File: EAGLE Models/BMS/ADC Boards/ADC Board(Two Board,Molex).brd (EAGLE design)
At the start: 77.5 x 64.4 mm, 34 parts, among them IC1 ADS7956, IC2 ADS7956, IC3 ADS7956, X1 6_PIN_CONNTE_IDC, X10 6_PIN_CONNTE_IDC, X11 6_PIN_CONNTE_IDC, X12 6_PIN_CONNTE_IDC, X2 6_PIN_CONNTE_IDC, X3 6_PIN_CONNTE_IDC, X4 6_PIN_CONNTE_IDC, X5 6_PIN_CONNTE_IDC, X6 6_PIN_CONNTE_IDC, X7 8_PIN_CONN

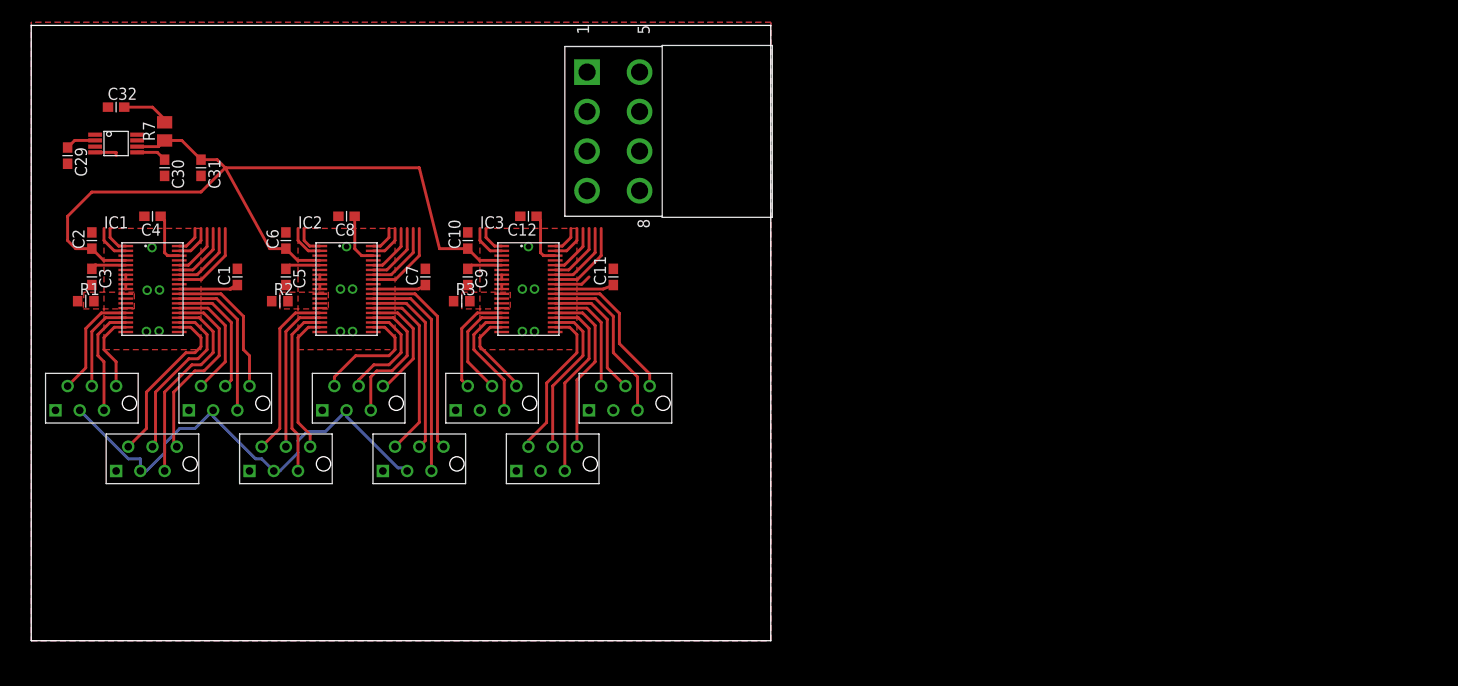
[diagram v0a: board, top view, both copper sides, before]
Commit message: Switched connectors, preparing to add dedicated analog power supply, Completed first revision of temp sense boards
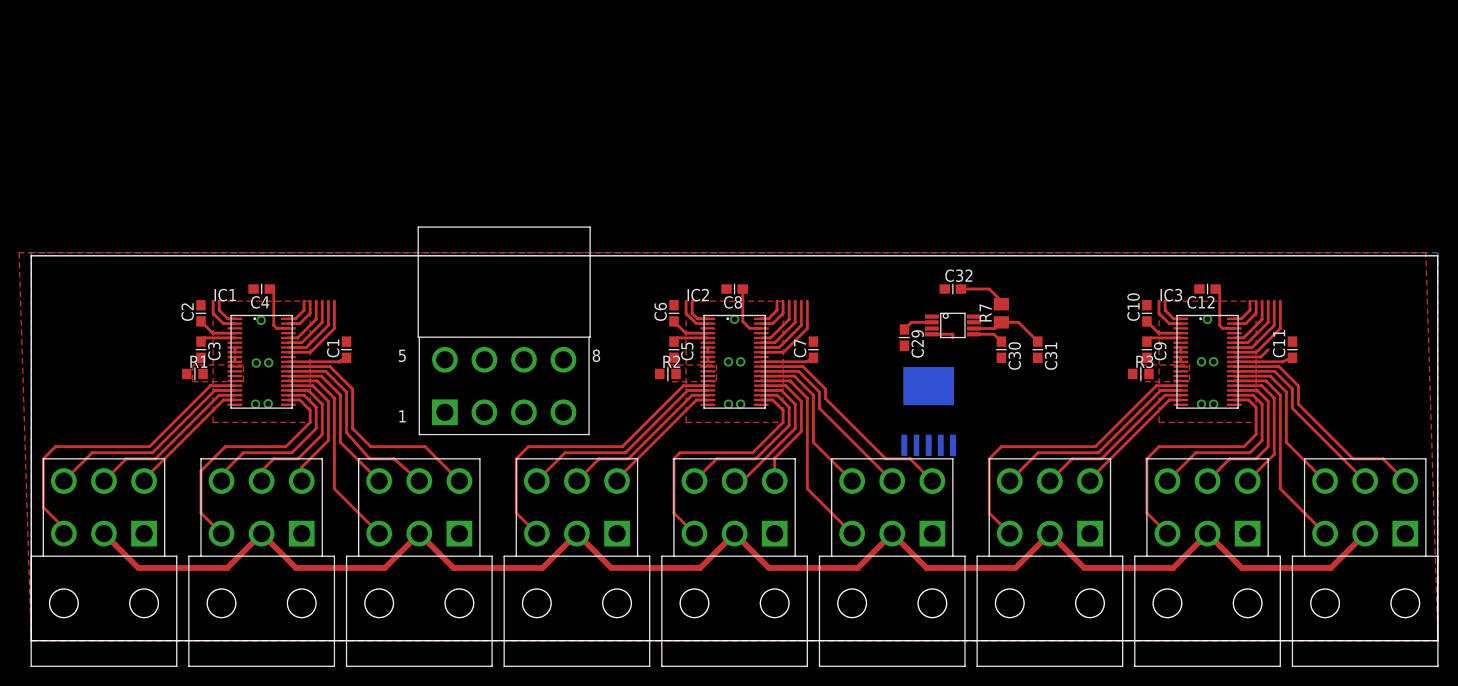
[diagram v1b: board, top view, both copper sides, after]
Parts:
- removed X11, X12: 6_PIN_CONNTE_IDC, BMS Lbr:2178710_IDC
- added U$2: REG-104GA-5, DashAndCAN library:REG104GA-5
- added X8, X9: 6_PIN_CONNMOLEX_HORI, BMS Lbr:6_PIN_MOLEX
- X1, X10, X2, X3, X4, X5, X6: value 6_PIN_CONNTE_IDC -> 6_PIN_CONNMOLEX_HORI; device BMS Lbr:2178710_IDC -> BMS Lbr:6_PIN_MOLEX
- moved C29 89.7 mm to (91.4, 31.8)
- moved C30 89.7 mm to (101.6, 30.5)
- moved C31 89.7 mm to (105.4, 30.5)
- moved C32 89.7 mm to (96.5, 36.8)
- moved R7 89.7 mm to (101.6, 34.3)
- moved U$1 89.7 mm to (96.5, 33.0)
- moved C10 71.5 mm to (116.8, 34.3)
- moved C11 71.5 mm to (132.1, 30.5)
- moved C12 71.5 mm to (123.2, 36.8)
- moved C9 71.5 mm to (116.8, 30.5)
- moved IC3 71.5 mm to (123.2, 29.2)
- moved R3 71.5 mm to (116.2, 27.9)
- moved X10 66.3 mm to (106.7, 14.0)
- moved C7 41.3 mm to (81.9, 30.5)
- moved C5 41.3 mm to (67.3, 30.5)
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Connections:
- new net N$1: U$2.VIN
- new net N$2: U$2.GND, U$2.HEATGND
- new net N$4: U$2.ENABLE
- new net N$5: U$2.VOUT
- net AIN0: now also X1.P$4; no longer X1.P$3
- net AIN1: now also X1.P$5; no longer X1.P$4
- net AIN10: now also X3.P$6; no longer X3.P$5
- net AIN11: now also X3.P$3; no longer X3.P$6
- net AIN12: now also X4.P$4; no longer X10.P$3
- net AIN13: now also X4.P$5; no longer X10.P$4
- net AIN14: now also X4.P$6; no longer X10.P$5
- net AIN15: now also X4.P$3; no longer X10.P$6
- net AIN16: now also X5.P$4; no longer X11.P$3
- net AIN17: now also X5.P$5; no longer X11.P$4
- net AIN18: now also X5.P$6; no longer X11.P$5
- net AIN19: now also X5.P$3; no longer X11.P$6
- net AIN2: now also X1.P$6; no longer X1.P$5
- net AIN20: now also X6.P$4; no longer X12.P$3
- net AIN21: now also X6.P$5; no longer X12.P$4
- net AIN22: now also X6.P$6; no longer X12.P$5
- net AIN23: now also X6.P$3; no longer X12.P$6
- net AIN24: now also X8.P$4; no longer X4.P$3
- net AIN25: now also X8.P$5; no longer X4.P$4
- net AIN26: now also X8.P$6; no longer X4.P$5
- net AIN27: now also X8.P$3; no longer X4.P$6
- net AIN28: now also X9.P$4; no longer X5.P$3
- net AIN29: now also X9.P$5; no longer X5.P$4
- net AIN3: now also X1.P$3; no longer X1.P$6
- net AIN30: now also X9.P$6; no longer X5.P$5
- net AIN31: now also X9.P$3; no longer X5.P$6
- net AIN32: now also X10.P$4; no longer X6.P$3
- net AIN33: now also X10.P$5; no longer X6.P$4
- net AIN34: now also X10.P$6; no longer X6.P$5
- net AIN35: now also X10.P$3; no longer X6.P$6
- net AIN4: now also X2.P$4; no longer X2.P$3
- net AIN5: now also X2.P$5; no longer X2.P$4
- net AIN6: now also X2.P$6; no longer X2.P$5
- net AIN7: now also X2.P$3; no longer X2.P$6
- net AIN8: now also X3.P$4; no longer X3.P$3
- net AIN9: now also X3.P$5; no longer X3.P$4
- net GND: now also X8.P$1, X9.P$1; no longer X11.P$1, X12.P$1
- net VA: now also X8.P$2, X9.P$2; no longer X11.P$2, X12.P$2
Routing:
- net VA: track 79.3 -> 185.0 mm
- net 2.5VREF: track 90.3 -> 20.0 mm
- net AIN35: track 11.2 -> 32.0 mm
- net AIN11: track 11.7 -> 32.0 mm
- net AIN23: track 18.0 -> 32.0 mm
- net AIN19: track 12.5 -> 25.7 mm
- net AIN10: track 9.86 -> 21.8 mm
- net AIN34: track 10.9 -> 21.8 mm
- net AIN31: track 16.4 -> 26.7 mm
- net AIN0: track 15.3 -> 25.3 mm
- net AIN27: track 12.1 -> 21.9 mm
- net AIN3: track 13.0 -> 21.7 mm
- net AIN24: track 16.5 -> 24.0 mm
- net AIN7: track 17.9 -> 25.0 mm
- net AIN18: track 11.6 -> 17.7 mm
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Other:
- board size 77.5 x 64.4 mm -> 147.3 x 40.3 mm

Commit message: CAN Board Layout
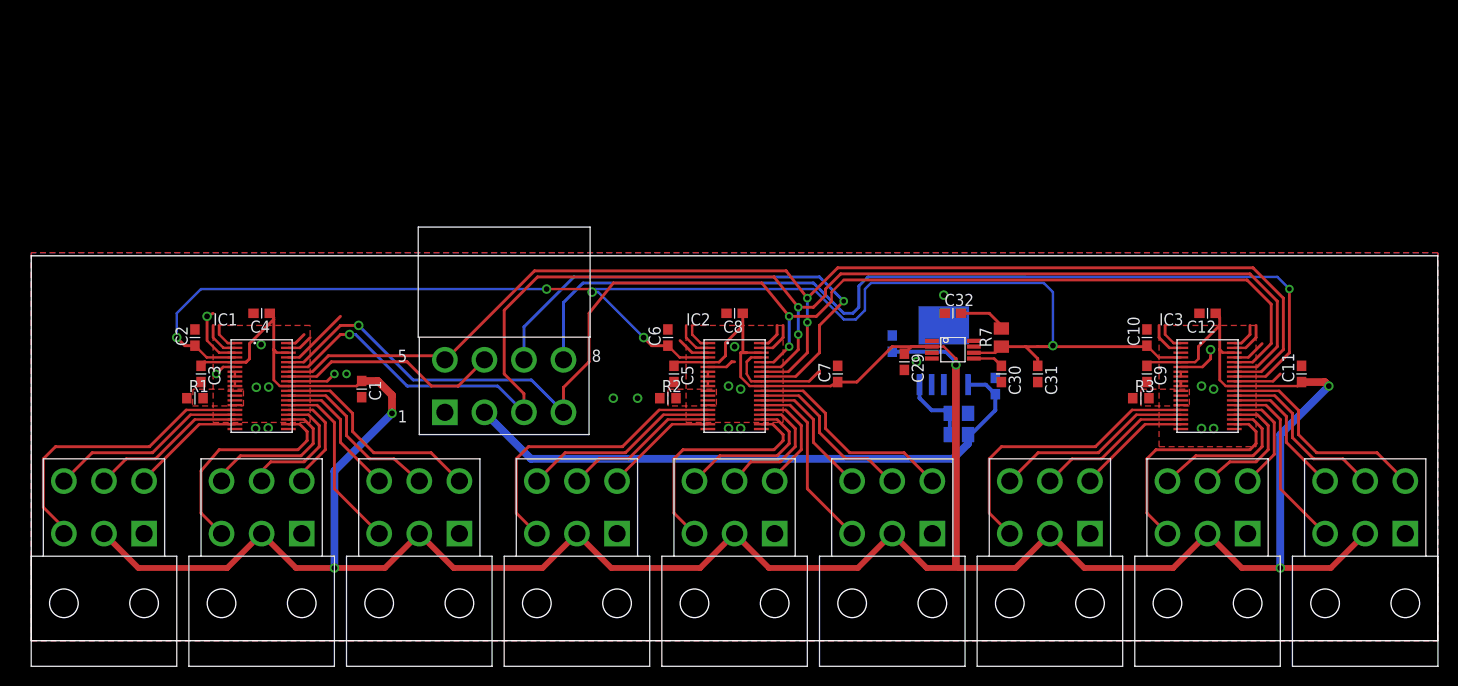
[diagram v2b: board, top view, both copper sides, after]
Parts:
- added C13, C14: .1uF, rcl:C0603
- added R4, R5: 100k, rcl:M0805
- moved U$2 6.55 mm to (95.6, 33.0)
- moved C1 4.42 mm to (34.6, 26.4), turned to 270 degrees
- moved C7 3.59 mm to (84.5, 27.9)
- moved C11 2.71 mm to (133.0, 27.9)
- moved C6 2.62 mm to (66.7, 31.8)
- moved C2 2.62 mm to (17.1, 31.8)
- moved R1 2.54 mm to (17.1, 25.4)
- moved R2 2.54 mm to (66.7, 25.4)
- moved R3 2.54 mm to (116.2, 25.4)
- moved U$1 2.54 mm to (96.5, 30.5)
- moved C10 2.54 mm to (116.8, 31.8)
- moved C12 2.54 mm to (123.2, 34.3)
- moved C29 2.54 mm to (91.4, 29.2)
- moved C3 2.54 mm to (17.8, 27.9)
- moved C30 2.54 mm to (101.6, 27.9)
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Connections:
- removed net N$1: U$2.VIN
- removed net N$2: U$2.GND, U$2.HEATGND
- removed net N$4: U$2.ENABLE
- removed net N$5: U$2.VOUT
- removed net VA: C1.1, C11.1, C3.1, C5.1, C7.1, C9.1, IC1.P$29, IC1.P$5, IC2.P$29, IC2.P$5, IC3.P$29, IC3.P$5, X1.P$2, X10.P$2, X2.P$2, X3.P$2, X4.P$2, X5.P$2, X6.P$2, X8.P$2, X9.P$2
- new net 12V: C14.1, R4.2, U$2.VIN, X7.P$2
- new net ENABLE: R4.1, R5.2, U$2.ENABLE
- net GND: now also C13.2, C14.2, R5.1, U$2.GND, U$2.HEATGND
- net VCC: now also C1.1, C11.1, C13.1, C3.1, C5.1, C7.1, C9.1, IC1.P$29, IC1.P$5, IC2.P$29, IC2.P$5, IC3.P$29, IC3.P$5, U$2.VOUT, X1.P$2, X10.P$2, X2.P$2, X3.P$2, X4.P$2, X5.P$2, X6.P$2, X8.P$2, X9.P$2; no longer X7.P$2
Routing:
- net VCC: track 20.1 -> 340.3 mm, vias 0 -> 5
- net VA: track 185.0 -> 0.00 mm
- net 2.5VREF: track 20.0 -> 154.3 mm, vias 0 -> 5
- net SDI: track 20.0 -> 147.1 mm, vias 0 -> 3
- net SDO: track 16.9 -> 139.0 mm, vias 0 -> 3
- net SCLK: track 23.0 -> 135.8 mm, vias 0 -> 2
- net CS2: track 8.71 -> 101.1 mm, vias 0 -> 1
- net 12V: track 0.00 -> 63.1 mm
- net GND: track 7.91 -> 54.2 mm, vias 15 -> 23
- net CS1: track 8.71 -> 53.7 mm, vias 0 -> 1
- net CS0: track 8.71 -> 23.4 mm
- net ENABLE: track 0.00 -> 7.42 mm
- net AIN4: track 14.4 -> 11.6 mm
- net AIN14: track 17.0 -> 14.4 mm
- net AIN2: track 17.0 -> 14.4 mm
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
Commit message: Moved things
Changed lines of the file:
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@@
 <wire x1="70.86" y1="28.67" x2="72.8025" y2="28.67" width="0.254" layer="1"/>
 <wire x1="72.8025" y1="28.67" x2="73.3425" y2="29.21" width="0.3048" layer="1"/>
-<wire x1="73.3425" y1="29.21" x2="73.66" y2="29.21" width="0.3048" layer="1"/>
 </signal>
 <signal name="SCLK">
